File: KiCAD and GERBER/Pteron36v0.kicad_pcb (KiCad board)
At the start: 2 copper layers, 140.1 x 108.1 mm, 56 parts, among them J1 AudioJack4, J2 AudioJack4, J3 Conn_01x04, SW10 SW_PUSH, SW12 SW_PUSH, SW13 SW_PUSH, SW14 SW_PUSH, SW15 SW_PUSH, SW17 SW_PUSH, SW18 SW_PUSH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

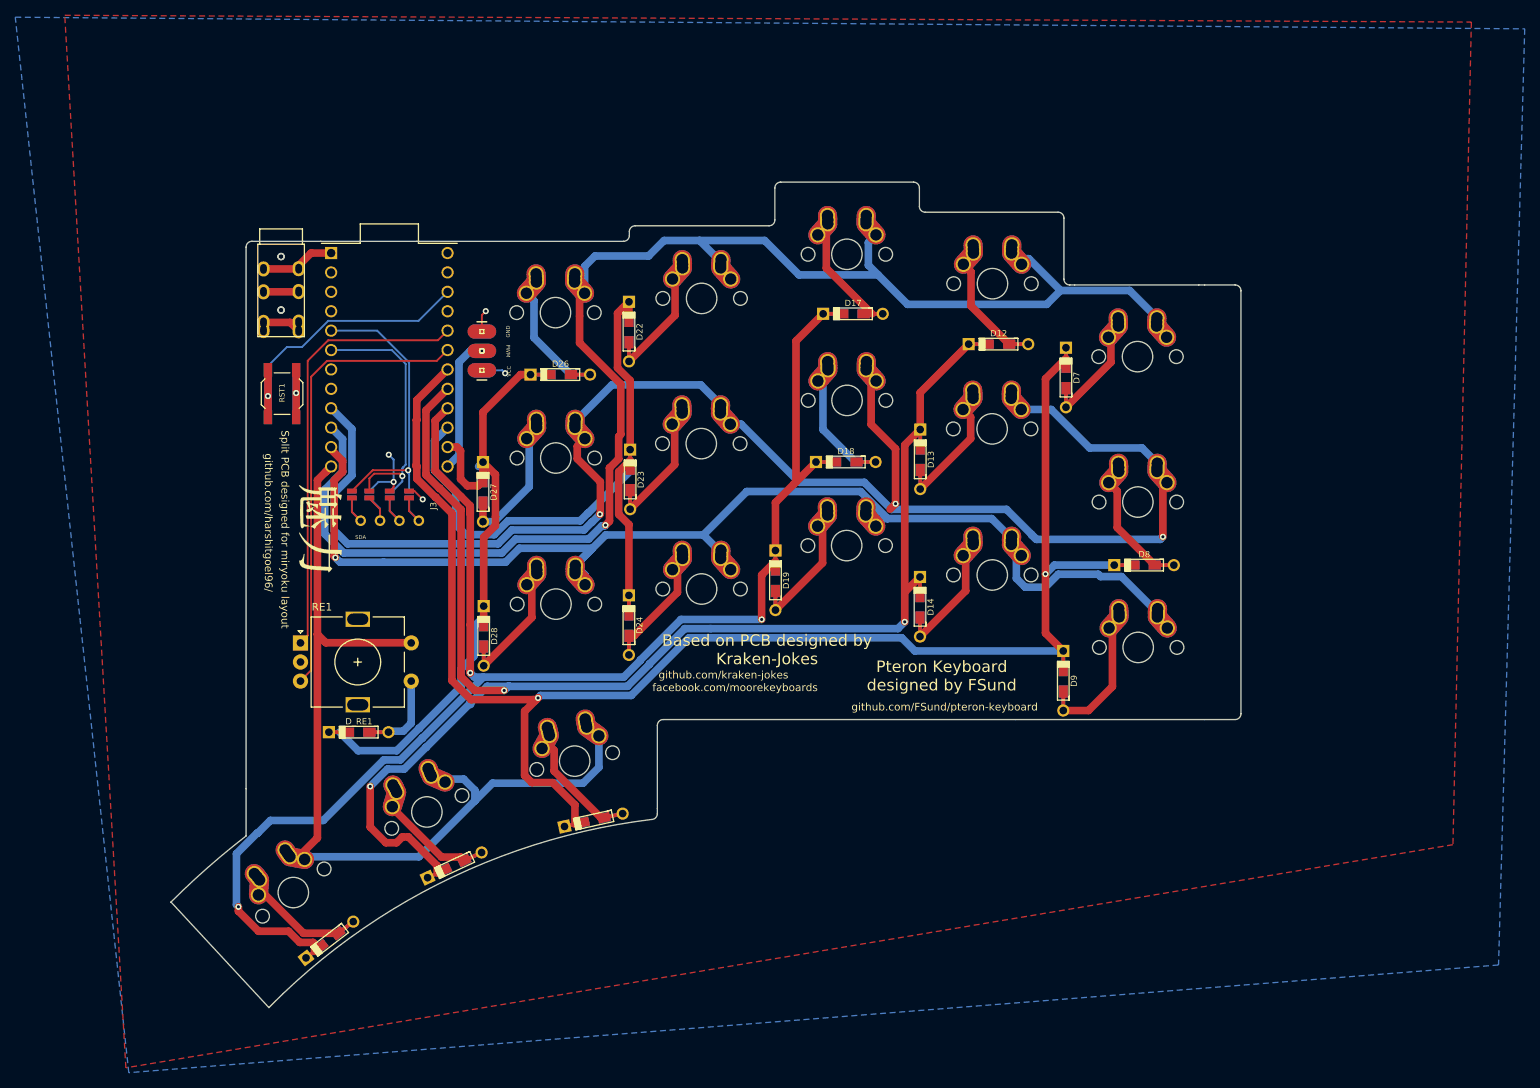
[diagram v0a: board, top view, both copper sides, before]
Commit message: added choc and mx support in single pcb.
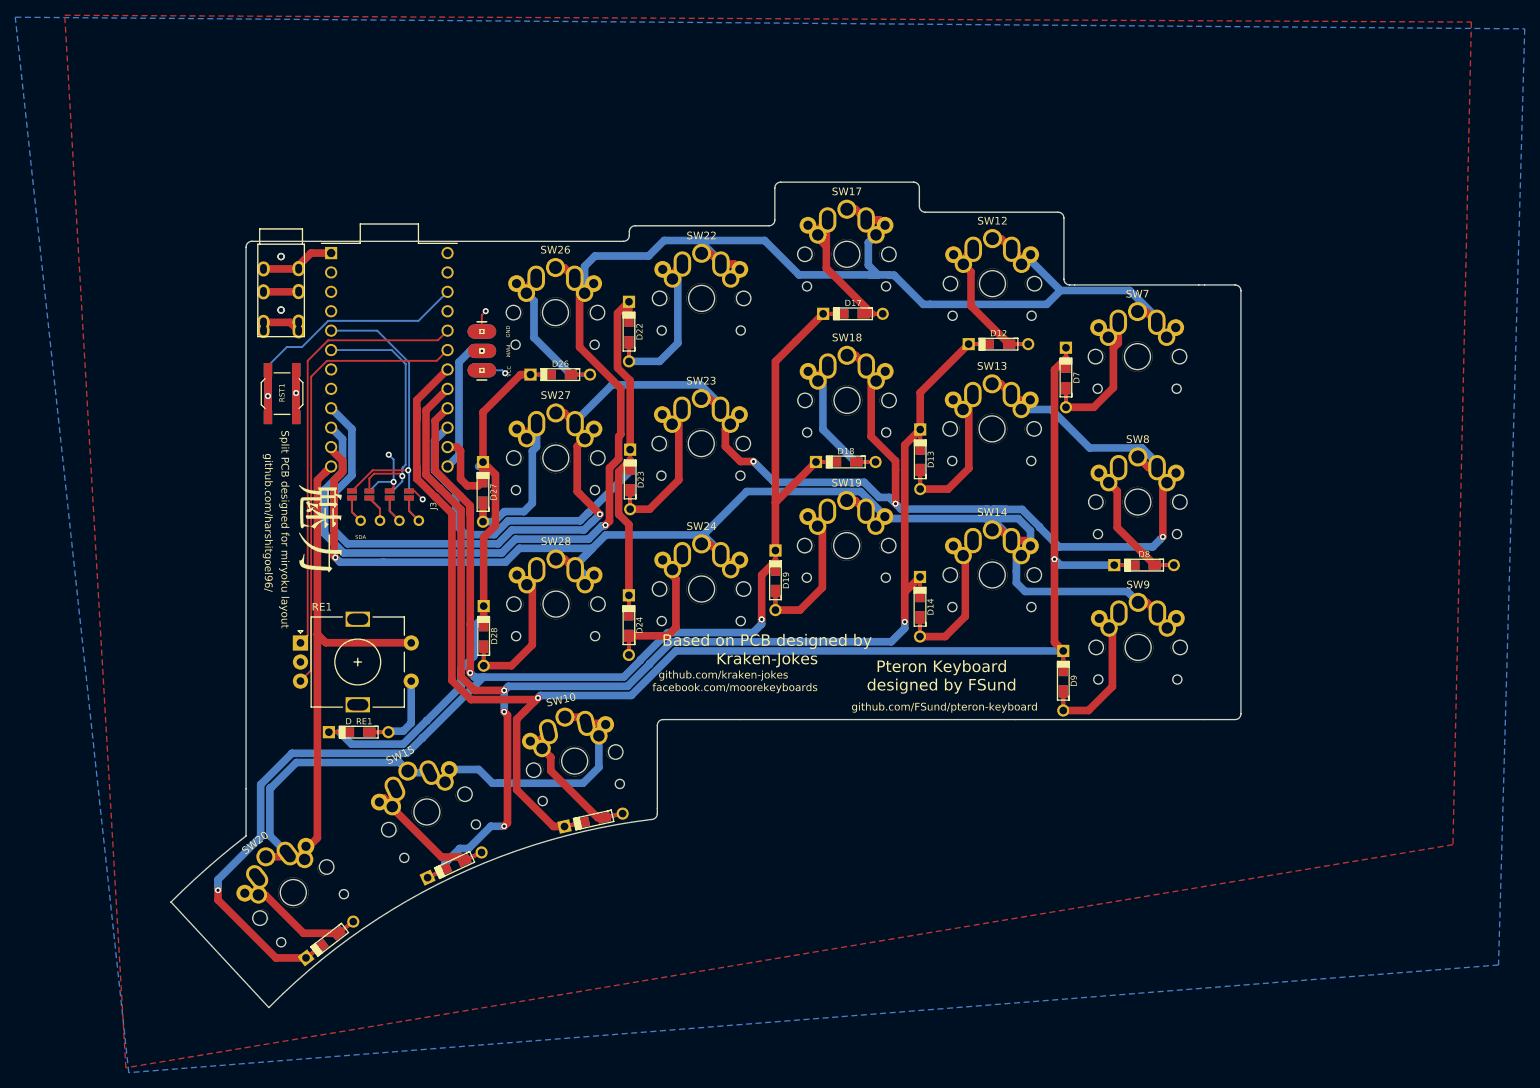
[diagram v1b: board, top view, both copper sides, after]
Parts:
- SW10, SW12, SW13, SW14, SW15, SW17, SW18, SW19, SW20, SW22, SW23, SW24, SW26, SW27, SW28, SW7, SW8, SW9: footprint Keebio-Parts:Hybrid_PCB_100H_Dual_hole -> Universal-Switch-Footprint:MX-ALPs-PG1350-FLIP
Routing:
- net /Row3: track 151.3 -> 193.1 mm
- net /Row2: track 201.5 -> 238.3 mm, vias 3 -> 4
- net /Row1: track 192.1 -> 227.9 mm
- net /Row4: track 122.3 -> 140.8 mm
- net /Col2: track 187.6 -> 175.2 mm, vias 3 -> 4
- net Net-(D22-Pad2): track 13.4 -> 22.8 mm
- net Net-(D7-Pad2): track 11.7 -> 20.4 mm
- net /Col3: track 188.8 -> 197.4 mm
- net Net-(D13-Pad2): track 13.6 -> 21.7 mm
- net Net-(D27-Pad2): track 15.9 -> 23.9 mm
- net Net-(D23-Pad2): track 13.7 -> 21.7 mm
- net Net-(D28-Pad2): track 13.9 -> 21.9 mm
- net Net-(D19-Pad2): track 14.3 -> 21.9 mm
- net Net-(D17-Pad2): track 14.4 -> 20.6 mm
- net Net-(D24-Pad2): track 12.4 -> 18.7 mm
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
